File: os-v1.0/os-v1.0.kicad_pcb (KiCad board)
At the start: 2 copper layers, 40 x 41 mm, 53 parts, among them J1 Conn_01x02, J2 Conn_01x04, Q1 2N7002, SW1 SW_Push, SW2 SW_Push, SW3 SW_Push, SW4 SW_Push, SW5 SW_Push, U1 DS3231MZ, U10 MCP1812AT, U11 MCP73831T-2ACI_OT, U2 BMA400, U3 BMP280, U4 GC9A01_IPS_display, U5 USB-OTG, U6 CH340E, U7 ttgo-32-micro, U8 Quectel_L96, U9 TPS2115A_default

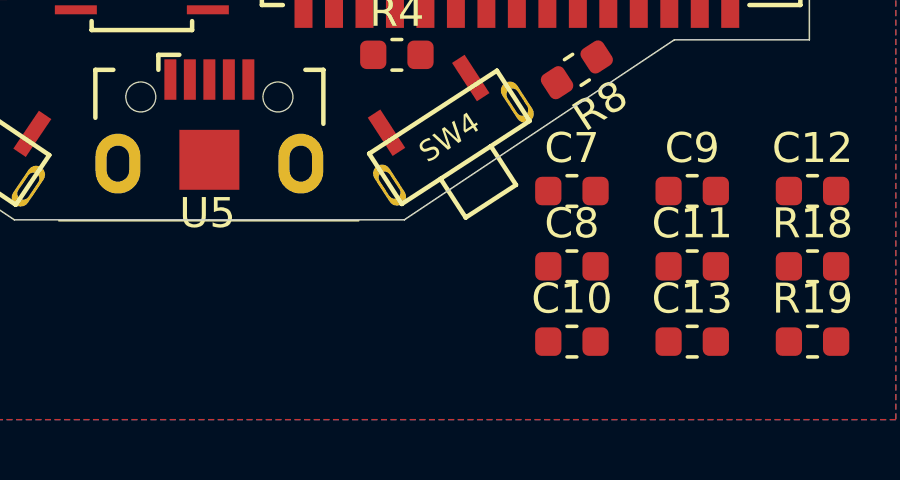
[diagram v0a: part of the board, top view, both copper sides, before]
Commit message: adds addl cap to ch240e and updates board and bom
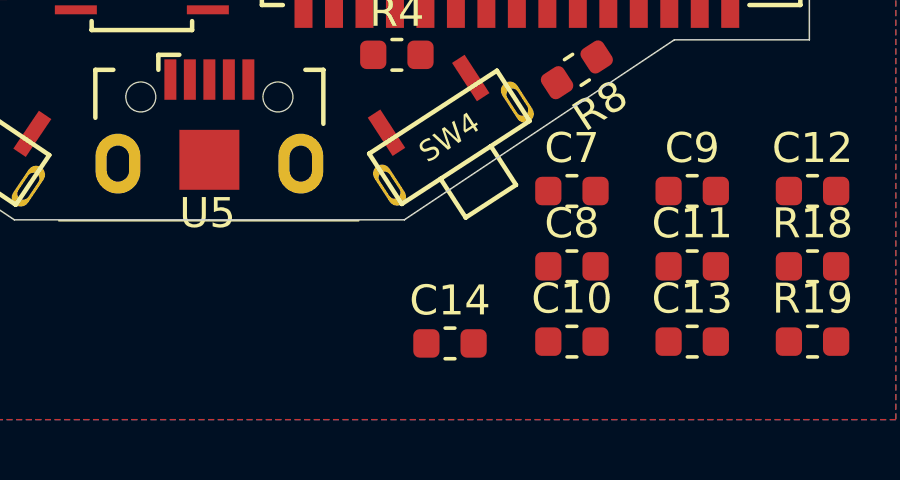
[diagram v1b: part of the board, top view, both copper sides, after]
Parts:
- added C14: 0.1u, Capacitor_SMD:C_0603_1608Metric, F.Cu at (168.0, 134.6)
- U4: value GC9A01_IPS_display -> GC9A01_IPS_display_SPI
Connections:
- net /VBAT renamed +BATT
- net /VBUS renamed VBUS
- net /VOUT renamed VDD
